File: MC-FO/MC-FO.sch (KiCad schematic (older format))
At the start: 17 parts, among them J1 86094327313755E1LF, U161 IFD97, U163 74LVC1G32SE-7, U164 74LVC1G0832DBVT

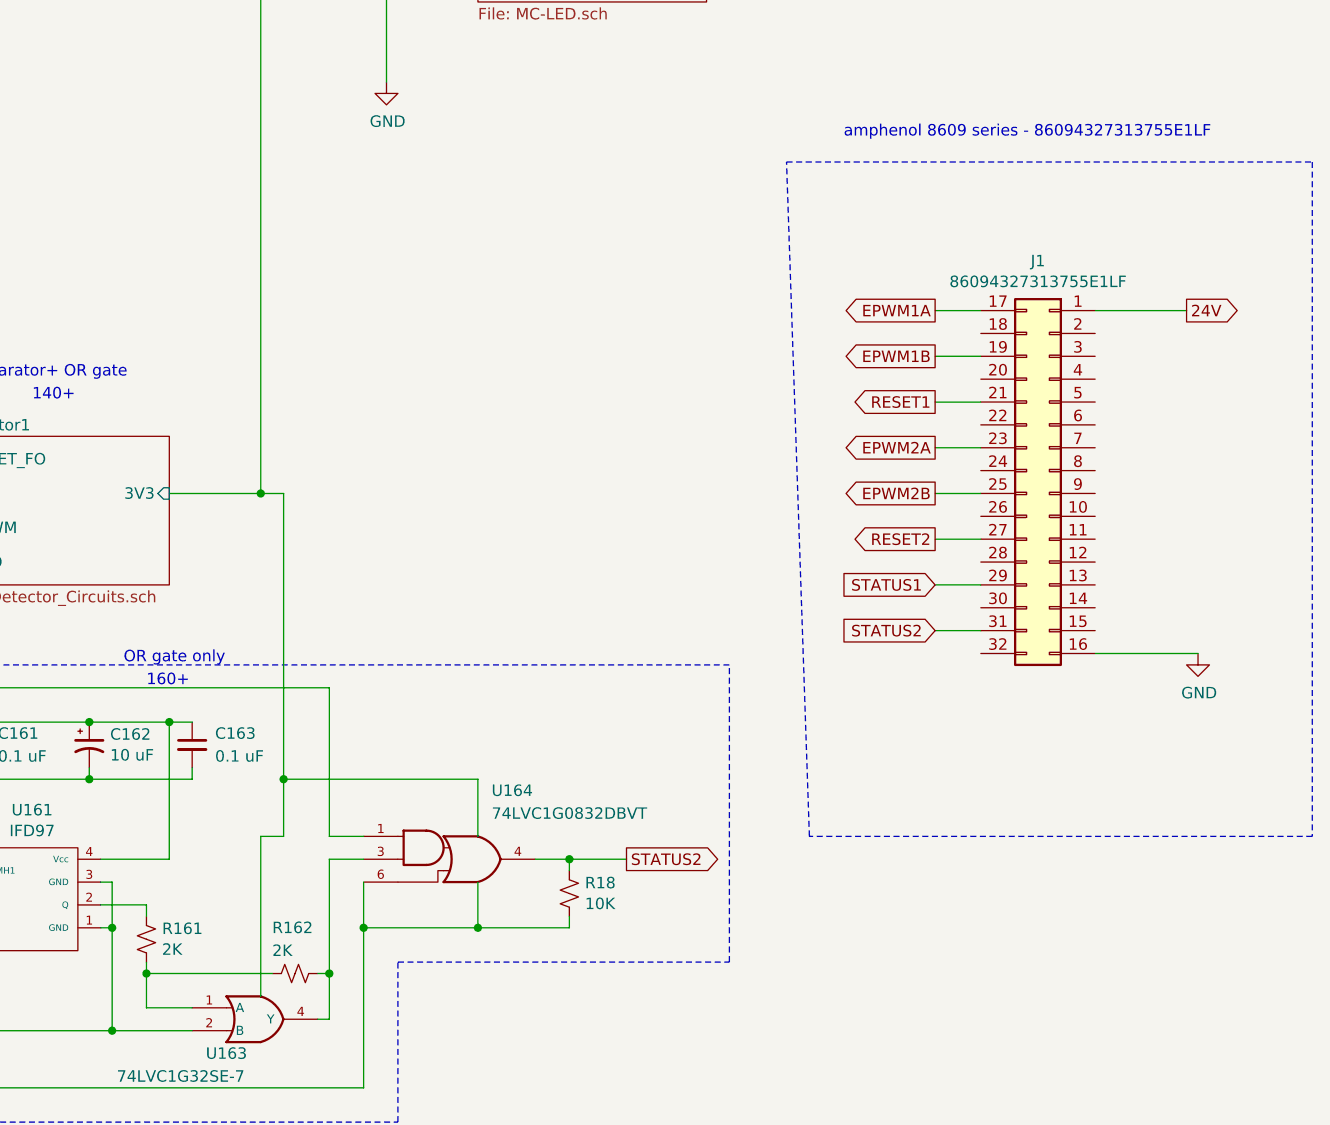
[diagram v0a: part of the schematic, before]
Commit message: Update LED, Transc. Footprint, layout
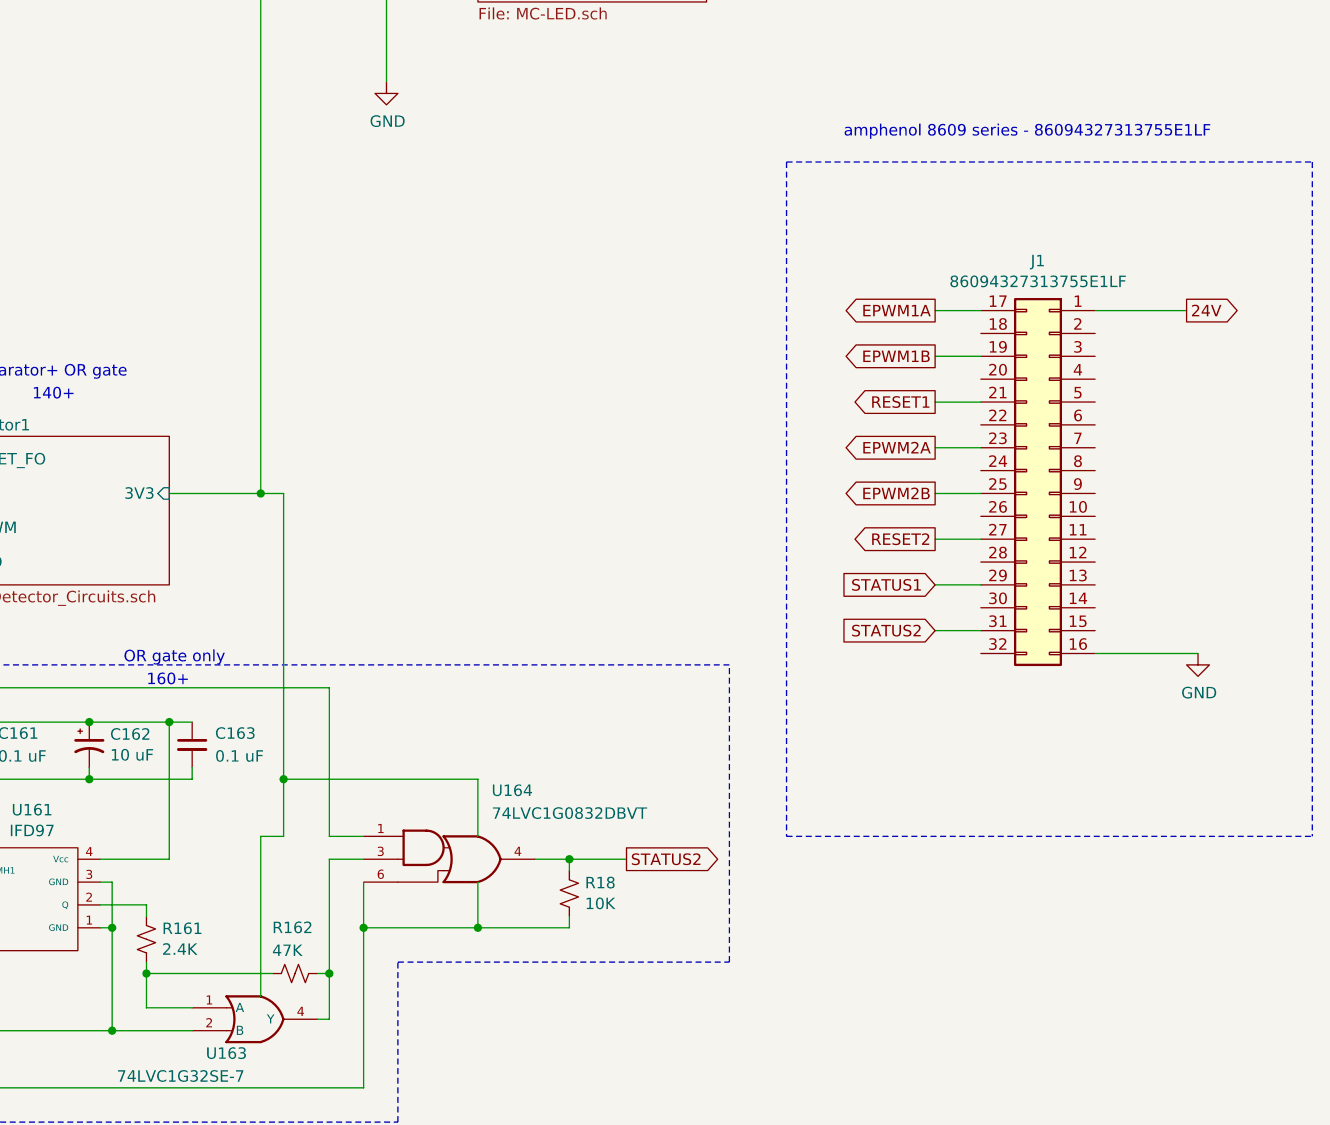
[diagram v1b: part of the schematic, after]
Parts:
- R161: value 2K -> 2.4K
- R162: value 2K -> 47K
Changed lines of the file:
@@
 Wire Notes Line
 	10800 2900 10800 5850
-Wire Notes Line
-	10800 5850 8600 5850
-Wire Notes Line
-	8600 5850 8500 2900
 Text Notes 650  1400 0    50   ~ 0
 20+
@@
 P 5700 6300
 F 0 "R161" H 5768 6346 50  0000 L CNN
-F 1 "2K" H 5768 6255 50  0000 L CNN
+F 1 "2.4K" H 5768 6255 50  0000 L CNN
 F 2 "Resistor_SMD:R_0603_1608Metric" H 5700 6300 50  0001 C CNN
 F 3 "~" H 5700 6300 50  0001 C CNN
@@
 P 6350 6450
 F 0 "R162" V 6150 6350 50  0000 L CNN
-F 1 "2K" V 6250 6350 50  0000 L CNN
+F 1 "47K" V 6250 6350 50  0000 L CNN
 F 2 "Resistor_SMD:R_0603_1608Metric" H 6350 6450 50  0001 C CNN
 F 3 "~" H 6350 6450 50  0001 C CNN
@@
 Wire Wire Line
 	10250 3550 9850 3550
+Wire Notes Line
+	8500 2900 8500 5850
+Wire Notes Line
+	8500 5850 10800 5850
 $EndSCHEMATC

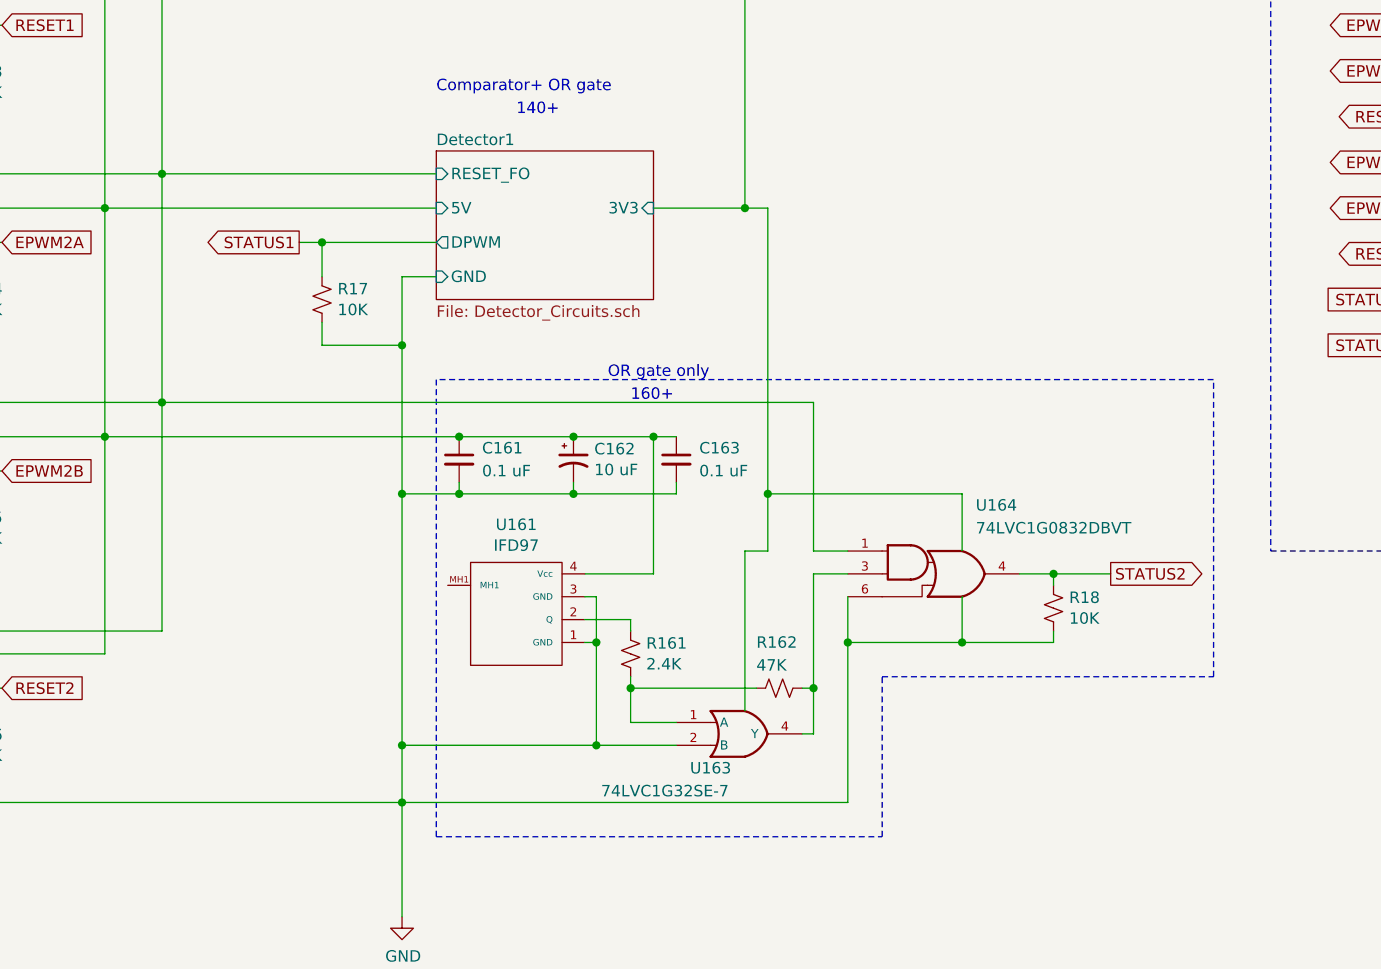
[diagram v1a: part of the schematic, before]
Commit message: Removed AND-OR gates
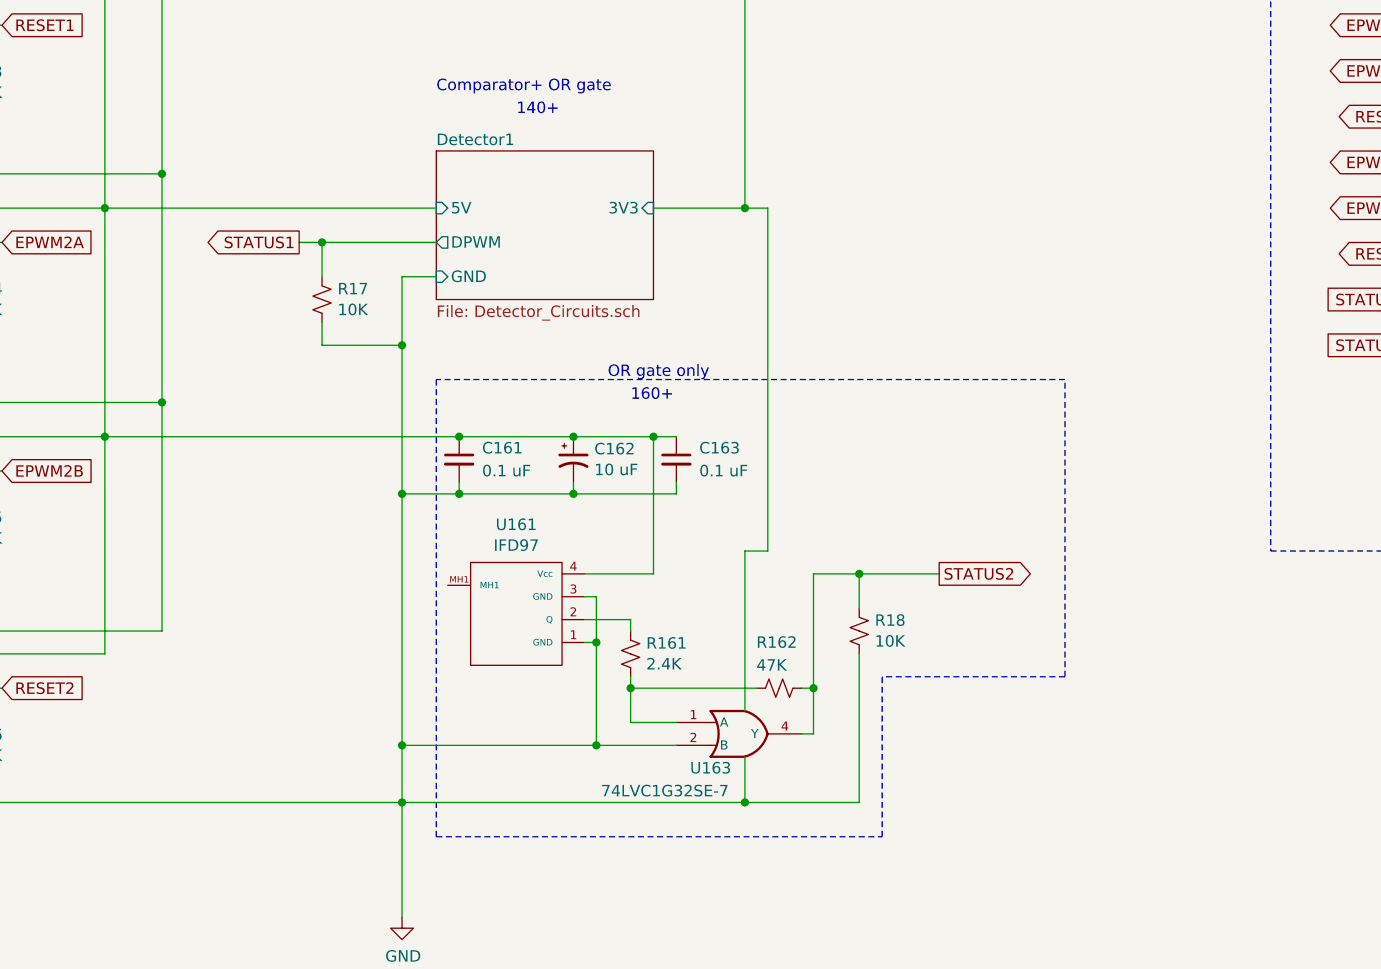
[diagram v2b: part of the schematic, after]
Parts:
- removed U164: 74LVC1G0832DBVT, Package_TO_SOT_SMD:SOT-23-6, symbol Existing_IC_Models:74LVC1G0832DBVT
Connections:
- net STATUS2: now also R162.1, U163.4 (Y)
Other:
- moved on the sheet: R18
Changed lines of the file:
@@
 F3 "5V" I L 4850 4350 50
 F4 "GND" I L 4850 4650 50
-F5 "RESET_FO" I L 4850 4200 50
-F6 "3V3" I R 5800 4350 50
+F5 "3V3" I R 5800 4350 50
 $EndSheet
 Wire Wire Line
@@
 Text GLabel 4250 4500 0    50   Output ~ 0
 STATUS1
-Text GLabel 7800 5950 2    50   Output ~ 0
+Text GLabel 7050 5950 2    50   Output ~ 0
 STATUS2
 Wire Wire Line
@@
 	2050 6200 3650 6200
 Wire Wire Line
-	4850 4200 3650 4200
-Wire Wire Line
 	2400 6600 2400 6950
 Wire Wire Line
@@
 Wire Wire Line
 	5800 5350 5800 5950
-Wire Wire Line
-	6500 5850 6500 5200
-Wire Wire Line
-	3650 5200 6500 5200
 Connection ~ 4700 6700
 Wire Wire Line
@@
 Connection ~ 6200 4350
 Wire Wire Line
-	4700 6950 6650 6950
-Wire Wire Line
 	4950 5350 3400 5350
 Connection ~ 4950 5350
@@
 L Device:R_Small_US R18
 U 1 1 6193B542
-P 7550 6100
-F 0 "R18" H 7618 6146 50  0000 L CNN
-F 1 "10K" H 7618 6055 50  0000 L CNN
-F 2 "Resistor_SMD:R_0603_1608Metric" H 7550 6100 50  0001 C CNN
-F 3 "~" H 7550 6100 50  0001 C CNN
-	1    7550 6100
-	1    0    0    -1
-$EndComp
-$Comp
-L Existing_IC_Models:74LVC1G0832DBVT U164
-U 1 1 6181E6F6
-P 7000 5950
-F 0 "U164" H 7300 6250 50  0000 C CNN
-F 1 "74LVC1G0832DBVT" H 7550 6150 50  0000 C CNN
-F 2 "Package_TO_SOT_SMD:SOT-23-6" H 7000 5950 50  0001 C CNN
-F 3 "http://www.ti.com/lit/sg/scyt129e/scyt129e.pdf" H 7000 5950 50  0001 C CNN
-	1    7000 5950
-	1    0    0    -1
-$EndComp
-Wire Wire Line
-	6500 5850 6650 5850
-Wire Wire Line
-	6500 5950 6650 5950
-Wire Wire Line
-	7150 5600 7150 5850
-Connection ~ 6650 6250
-Wire Wire Line
-	6650 6250 6650 6950
-Wire Wire Line
-	6650 6050 6650 6250
-Wire Wire Line
-	6650 6250 7150 6250
-Wire Wire Line
-	7400 5950 7550 5950
-Wire Wire Line
-	7550 6000 7550 5950
-Connection ~ 7550 5950
-Wire Wire Line
-	7550 5950 7800 5950
-Wire Wire Line
-	7550 6200 7550 6250
-Wire Wire Line
-	7150 6050 7150 6250
-Connection ~ 7150 6250
-Wire Wire Line
-	7150 6250 7550 6250
+P 6700 6200
+F 0 "R18" H 6768 6246 50  0000 L CNN
+F 1 "10K" H 6768 6155 50  0000 L CNN
+F 2 "Resistor_SMD:R_0603_1608Metric" H 6700 6200 50  0001 C CNN
+F 3 "~" H 6700 6200 50  0001 C CNN
+	1    6700 6200
+	1    0    0    -1
+$EndComp
 Connection ~ 2400 2900
 Wire Wire Line
@@
 	6800 7100 6800 6400
 Wire Notes Line
-	8250 6400 8250 5100
-Wire Notes Line
-	8250 5100 4850 5100
+	7600 6400 7600 5100
 Wire Notes Line
 	4850 5100 4850 7100
 Wire Notes Line
-	6800 6400 8250 6400
-Wire Notes Line
 	4850 7100 6800 7100
 Wire Wire Line
 	6200 4350 6300 4350
 Wire Wire Line
-	6300 4350 6300 5600
-Wire Wire Line
-	6300 5600 7150 5600
-Wire Wire Line
 	6200 5850 6200 6550
 Wire Wire Line
-	6300 5600 6300 5850
-Wire Wire Line
 	6300 5850 6200 5850
-Connection ~ 6300 5600
 Wire Wire Line
 	9350 3550 9150 3550
@@
 Wire Notes Line
 	8500 5850 10800 5850
+Wire Wire Line
+	6300 4350 6300 5850
+Wire Notes Line
+	7600 5100 4850 5100
+Wire Notes Line
+	7600 6400 6800 6400
+Wire Wire Line
+	6500 5950 6700 5950
+Wire Wire Line
+	6700 6300 6700 6950
+Wire Wire Line
+	4700 6950 6200 6950
+Wire Wire Line
+	6700 6100 6700 5950
+Connection ~ 6700 5950
+Wire Wire Line
+	6700 5950 7050 5950
+Wire Wire Line
+	6200 6750 6200 6950
+Connection ~ 6200 6950
+Wire Wire Line
+	6200 6950 6700 6950
 $EndSCHEMATC
